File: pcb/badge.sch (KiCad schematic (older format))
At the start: 12 parts, among them IC1 ATTINY48-A, IC2 AAT3681A, P1 CONN_02X07, P2 CONN_01X06, P3 CONN_01X02, P4 USB_OTG

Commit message: started work on the hat edition
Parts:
- removed C1: C, netl:SMD_0603, symbol C
- removed D1: D, netl:SMD_0603, symbol D
- removed D2: LED, netl:SMD_0603, symbol LED
- removed IC1: ATTINY48-A, Housings_QFP:TQFP-32_7x7mm_Pitch0.8mm, symbol ATTINY48-A
- removed P1: CONN_02X07, netl:8x2_backlight, symbol CONN_02X07
- removed P2: CONN_01X06, Pin_Headers:Pin_Header_Straight_1x06, symbol CONN_01X06
- removed R1: R, netl:SMD_0603, symbol R
- removed R3: 0R, symbol R
- added C101, C102, C103, C104: C, netl:SMD_0603, symbol C
- added C105: 100n, netl:SMD_0603, symbol C
- added D101: LED, netl:SMD_0603, symbol LED
- added IC101: ATMEGA8-AI, Housings_QFP:TQFP-32_7x7mm_Pitch0.8mm, symbol ATMEGA8-AI
- added P101: CONN_02X03, Pin_Headers:Pin_Header_Straight_2x03, symbol CONN_02X03
- added P104, P105, P106, P107, P108, P109: CONNECTOR, netl:1Pin_small, symbol CONNECTOR
- added Q101: FT230XS-R, Housings_SSOP:SSOP-16_5.3x6.2mm_Pitch0.65mm, symbol FT230XS-R
- added Q102: NPN, TO_SOT_Packages_SMD:SOT-323, symbol NPN
- added R101: 10k, netl:SMD_0603, symbol R
- added R102, R103, R106, R107, R108: R, netl:SMD_0603, symbol R
- added SW101: SW_PUSH, Buttons_Switches_SMD:SW_SPST_EVQPE1, symbol SW_PUSH
- added Y101: Crystal, Crystals:Crystal_HC49-U_Vertical, symbol Crystal
- renumbered IC2 to IC102, P3 to P102, P4 to P103, R2 to R105
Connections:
- net GND: now also C101.2, C102.2, C103.2, C104.2, D101.1 (K), IC101.21 (AGND), IC101.3 (GND), IC101.5 (GND), P101.6 (P6), Q101.13 (GND), Q101.5 (GND), R107.2, SW101.2
- net MISO: now also IC101.16 ((MISO)PB4), P101.1 (P1)
- net MOSI: now also IC101.15 ((MOSI/OC2)PB3), P101.4 (P4)
- net SCK: now also IC101.17 ((SCK)PB5), P101.3 (P3)
- net VDD: now also C103.1, IC101.4 (VCC), IC101.6 (VCC), R101.1, R102.1; no longer IC102.3 (BAT), P102.1 (P1)
- net V_USB: now also IC102.4 (ADP), C104.1, Q101.12 (VCC)
- net ~RESET: now also C105.1, IC101.29 (PC6(~RESET~)), P101.5 (P5), R101.2
- net chrg: now reaches IC102.5 (STAT)
- net chrg: now also IC101.32 ((INT0)PD2)
- net D-: now reaches P103.2 (D-)
- net D-: now also Q101.9 (USBDM)
- net D+: now reaches P103.3 (D+)
- net D+: now also Q101.8 (USBDP)
- new net: IC101.12 ((ICP)PB0), SW101.1
- new net: IC101.13 ((OC1A)PB1), R103.2
- new net: IC101.23 ((ADC0)PC0), P104.1 (W)
- new net: IC101.24 ((ADC1)PC1), P105.1 (W)
- new net: IC101.25 ((ADC2)PC2), P106.1 (W)
- new net: IC101.26 ((ADC3)PC3), P107.1 (W)
- new net: IC101.27 ((ADC4/SDA)PC4), P108.1 (W)
- new net: IC101.28 ((ADC5/SCL)PC5), P109.1 (W)
- new net: C101.1, IC101.7 (PB6(XTAL1/TOSC1)), Y101.1
- new net: C102.1, IC101.8 (PB7(XTAL2/TOSC2)), Y101.2
- new net: P101.2 (P2), R102.2
- new net: D101.2 (A), R103.1
- new net: Q101.1 (TXD), R106.2
- new net: C105.2, Q101.2 (~RTS)
- new net: Q101.4 (RXD), Q102.2 (E), R107.1
- new net: Q102.1 (B), R108.2
- new net 3V3: Q101.10 (3V3OUT), Q101.11 (~RESET), Q101.3 (VCCIO), R108.1
- new net AVR_RX: IC101.30 ((RXD)PD0), R106.1
- new net AVR_TX: IC101.31 ((TXD)PD1), Q102.3 (C)
- new net VBat: IC102.3 (BAT), P102.1 (P1)
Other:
- moved on the sheet: IC102, P102, P103, R105

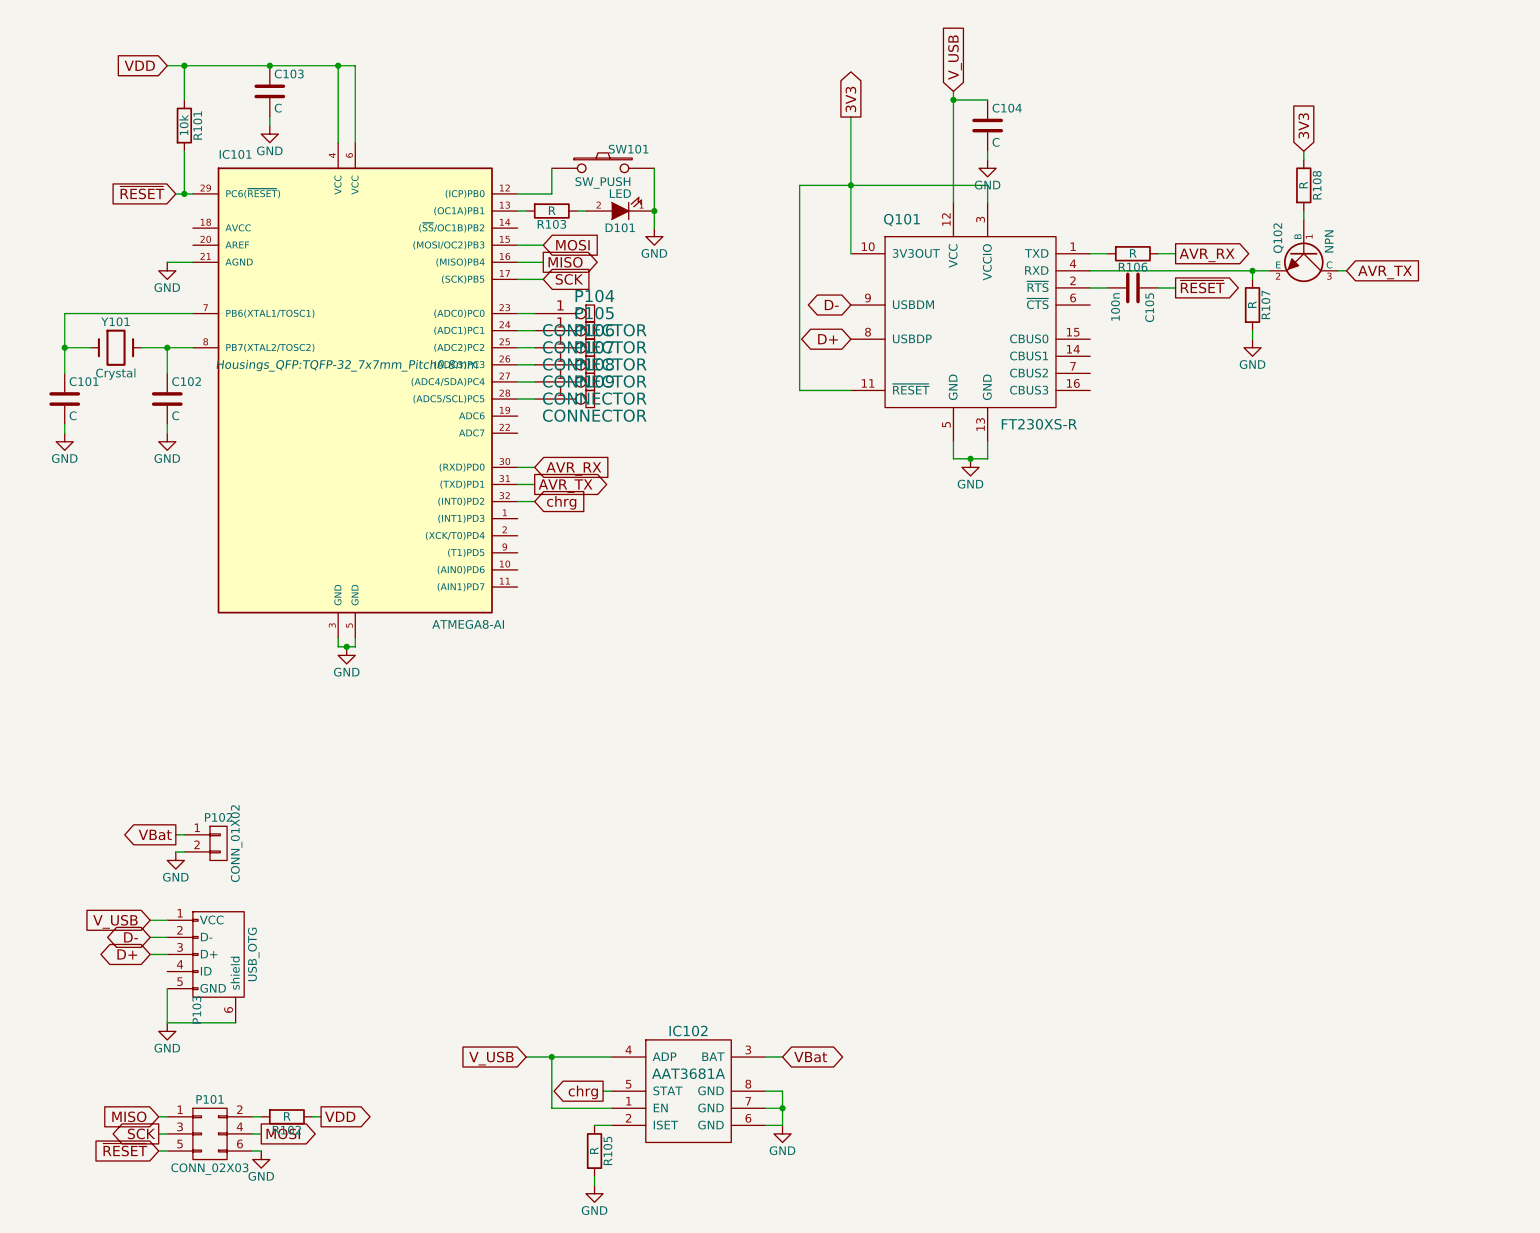
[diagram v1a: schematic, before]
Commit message: now just a plain serial programmer with a lipo charger
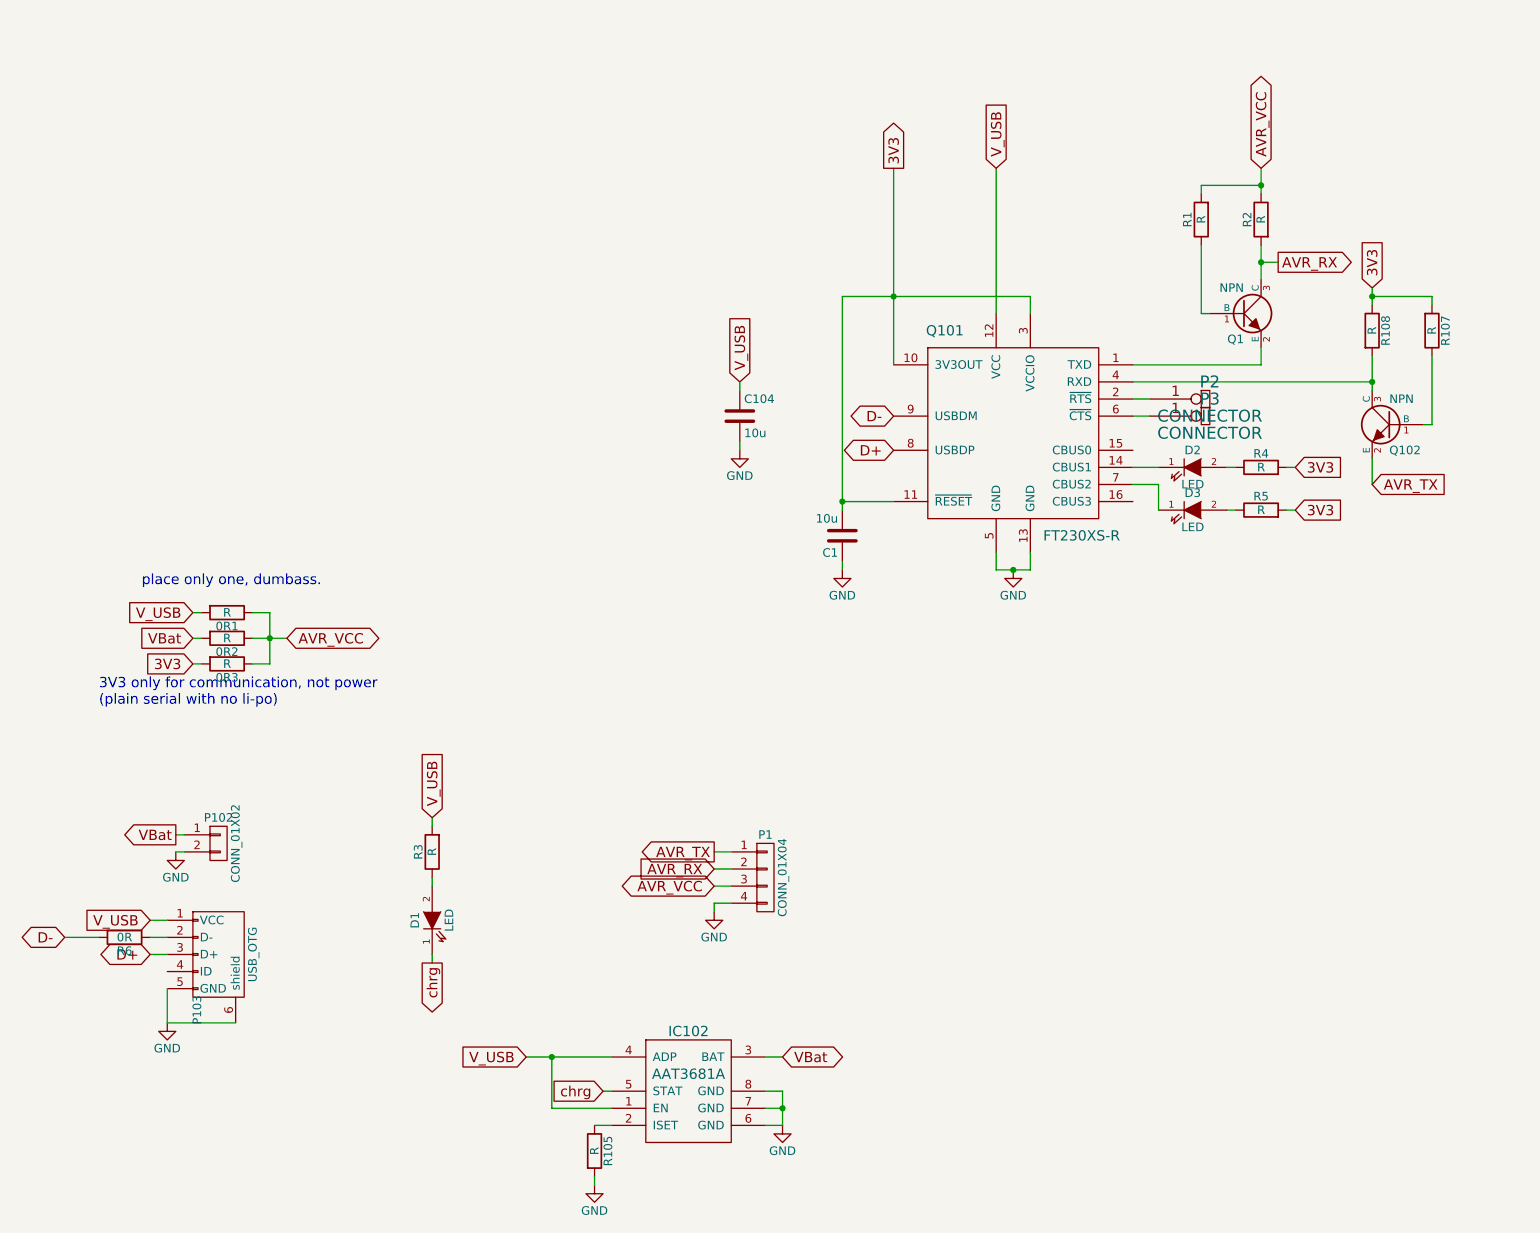
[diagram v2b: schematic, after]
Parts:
- removed C101, C102, C103: C, netl:SMD_0603, symbol C
- removed C105: 100n, netl:SMD_0603, symbol C
- removed D101: LED, netl:SMD_0603, symbol LED
- removed IC101: ATMEGA8-AI, Housings_QFP:TQFP-32_7x7mm_Pitch0.8mm, symbol ATMEGA8-AI
- removed P101: CONN_02X03, Pin_Headers:Pin_Header_Straight_2x03, symbol CONN_02X03
- removed P104, P105, P106, P107, P108, P109: CONNECTOR, netl:1Pin_small, symbol CONNECTOR
- removed R101: 10k, netl:SMD_0603, symbol R
- removed R102, R103, R106: R, netl:SMD_0603, symbol R
- removed SW101: SW_PUSH, Buttons_Switches_SMD:SW_SPST_EVQPE1, symbol SW_PUSH
- removed Y101: Crystal, Crystals:Crystal_HC49-U_Vertical, symbol Crystal
- added 0R1, 0R2, 0R3, R1, R2, R3, R4, R5: R, netl:SMD_0603, symbol R
- added C1: 10u, netl:SMD_0603, symbol C
- added D1, D2, D3: LED, netl:SMD_0603, symbol LED
- added P1: CONN_01X04, Pin_Headers:Pin_Header_Angled_1x04, symbol CONN_01X04
- added P2, P3: CONNECTOR, netl:1Pin_small, symbol CONNECTOR
- added Q1: NPN, TO_SOT_Packages_SMD:SOT-323, symbol NPN
- added R6: 0R, netl:SMD_0603, symbol R
- C104: value C -> 10u
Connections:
- net 3V3: now also R107.2, 0R3.2, C1.2, R4.2, R5.2
- net AVR_RX: now also P1.2 (P2), Q1.3 (C), R2.2
- net AVR_TX: now also Q102.2 (E), P1.1 (P1); no longer Q102.3 (C)
- net D-: now also R6.2; no longer P103.2 (D-)
- net GND: now also C1.1, P1.4 (P4); no longer R107.2
- net VBat: now also 0R2.2
- net V_USB: now also 0R1.2, R3.2
- net chrg: now also D1.1 (K)
- net at Q101.1 (TXD): now also Q1.2 (E)
- net at Q101.14 (CBUS1): now also D2.1 (K)
- net at Q101.2 (~RTS): now also P2.1 (W)
- net at Q101.6 (~CTS): now also P3.1 (W)
- net at Q101.7 (CBUS2): now also D3.1 (K)
- net at R108.2: now also Q101.4 (RXD), Q102.3 (C); no longer Q102.1 (B)
- new net: P103.2 (D-), R6.1
- new net: Q1.1 (B), R1.1
- new net: Q102.1 (B), R107.1
- new net: D1.2 (A), R3.1
- new net: D3.2 (A), R5.1
- new net: D2.2 (A), R4.1
- new net AVR_VCC: 0R1.1, 0R2.1, 0R3.1, P1.3 (P3), R1.2, R2.1
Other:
- note added: "3V3 only for communication, not power\n(plain serial with no li-po)"
- note added: "place only one, dumbass."
- moved on the sheet: C104, Q101, Q102, R107, R108
